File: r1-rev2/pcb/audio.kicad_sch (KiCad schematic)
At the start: 24 parts, among them J4 HP_3.5mm, J5 LO_3.5mm, Q2 AO3401A, Q3 AO3401A, U6 TLV320AIC3104

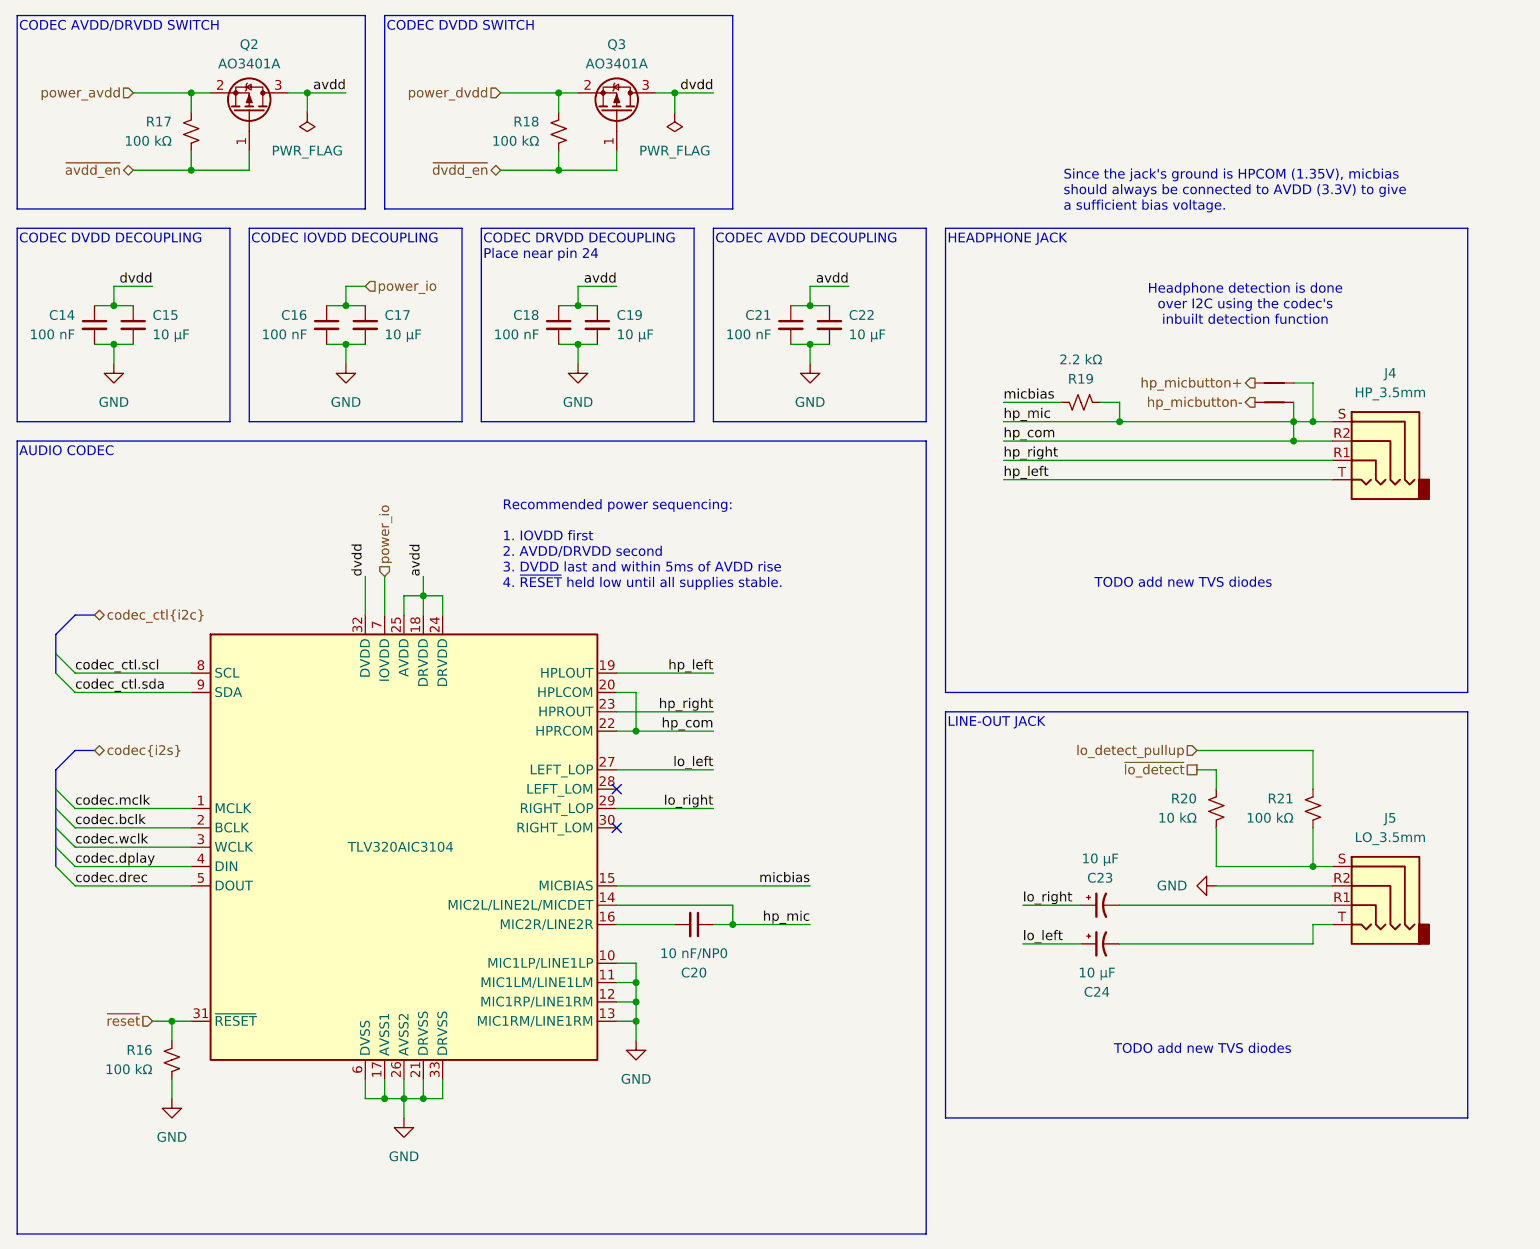
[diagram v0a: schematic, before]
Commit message: R1-Rev2: optimize resistor values
- Resistors used for the ADC dividers were way too high; I didn't
  take into account how the RC constant affected ADC performance
  so the conversion accuracy was probably poor. The new values are
  based on ST's recommendations and the theoretical resolution is
  computed in a spreadsheet.
- Simplify LO detect, originally I had the idea of a "wake on jack
  insert" feature but this is not possible for the headphone jack
  because it is only polled over I2C. The reason for the big 1M
  resistor that was there in Rev1 was to keep the effect on ground
  minimal. If the MCU is powered up then a simple hi-z input with
  internal pullup does the job better.
- Standardize on just 4 unique resistor values to reduce the cost
  of assembly: 5.1k is needed for USB, 2.2k for micbias and battery
  charge reference, and 15k and 68k for voltage reference. Other
  resistors have been rounded to one of these.
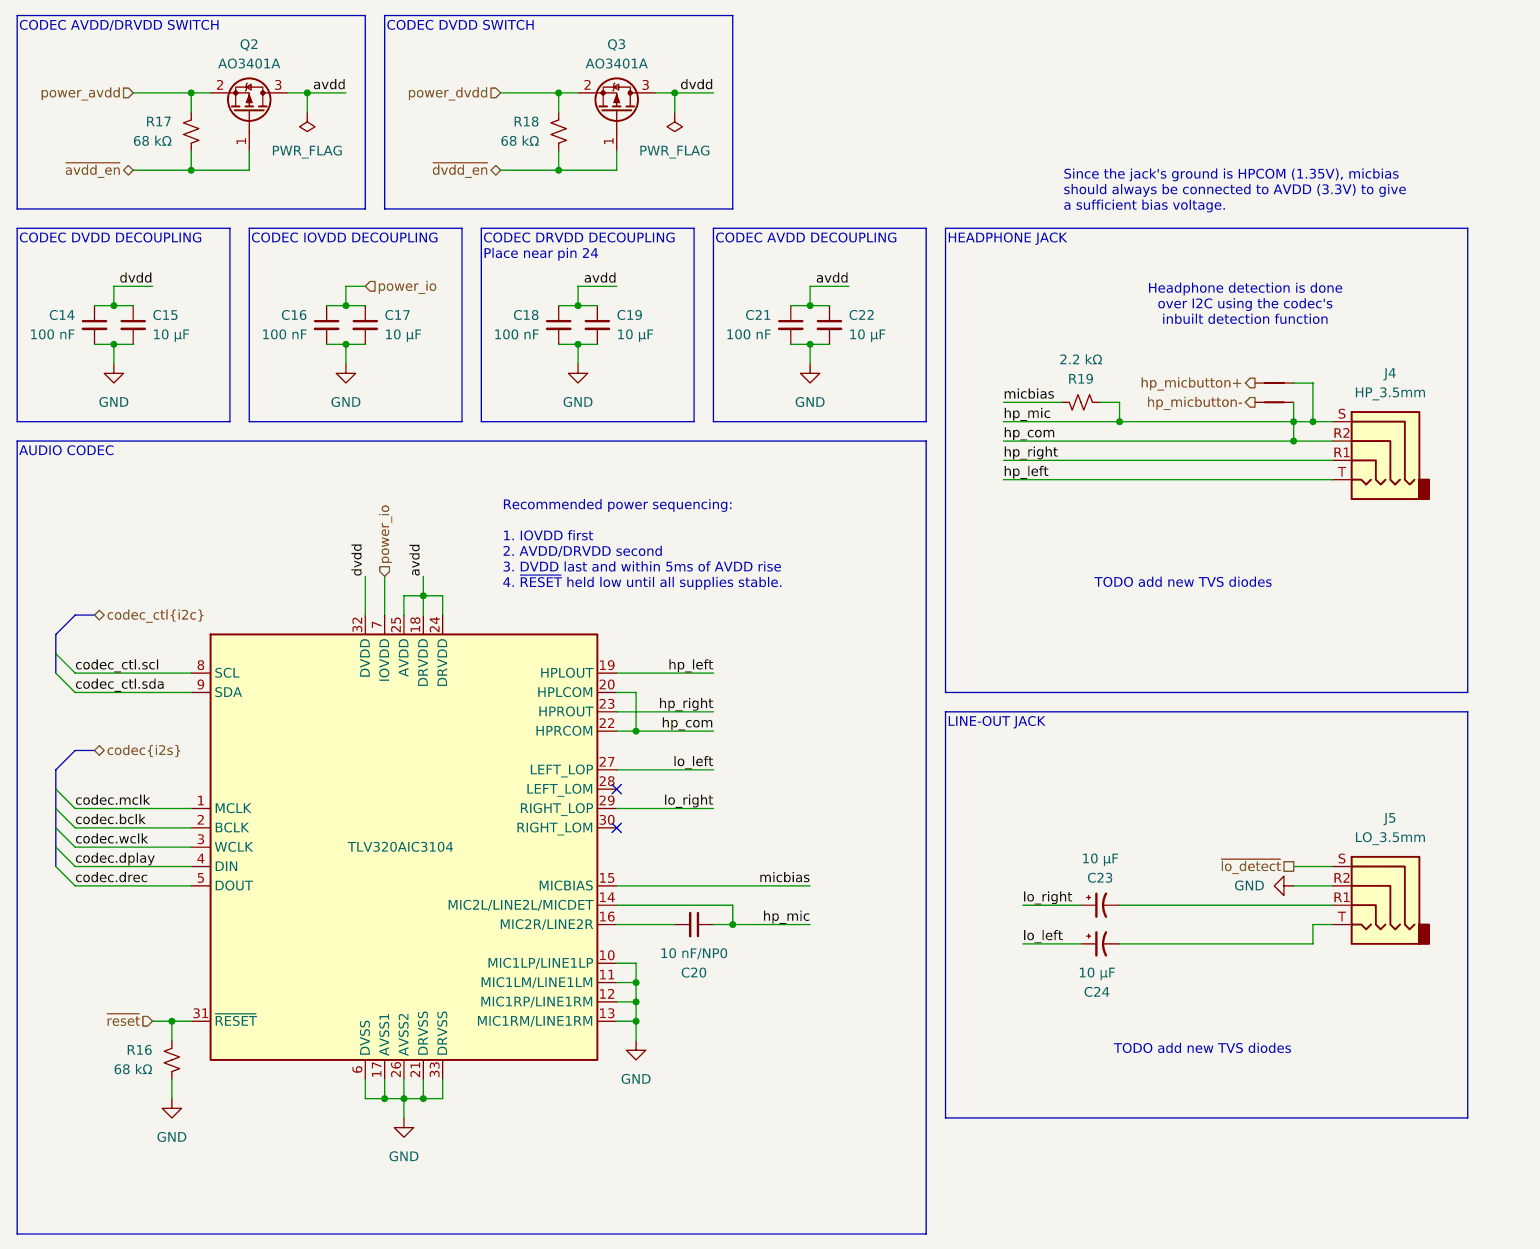
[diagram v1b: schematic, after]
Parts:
- removed R20: 10 kΩ, Resistor_SMD:R_0402_1005Metric, symbol Device:R_Small_US
- removed R21: 100 kΩ, Resistor_SMD:R_0402_1005Metric, symbol Device:R_Small_US
- R16, R17, R18: value 100 kΩ -> 68 kΩ
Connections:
- net ~{lo_detect}: now also J5.S

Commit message: R1-Rev2: strip LCSC part numbers from schematic
These will be managed in a separate BOM spreadsheet going forward.
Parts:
- C14, C16, C18, C21: LCSC# C77020 -> (none)
- C15, C17, C19, C22: LCSC# C91606 -> (none)
- C20: LCSC# C85973 -> (none)
- C23, C24: LCSC# C72485 -> (none)
- J4, J5: LCSC# C5372851 -> (none)
- Q2, Q3: LCSC# C347476 -> (none)
- R16, R17, R18: LCSC# C60491 -> (none)
- R19: LCSC# C114762 -> (none)
- U6: LCSC# C181753 -> (none)
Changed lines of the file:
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@@
-			)
-		)
-		(property "LCSC#" "C77020"
-			(at 93.98 55.88 0)
-			(effects
-				(font
-					(size 1.27 1.27)
-				)
-				(hide yes)
 			)
 		)
@@
 		)
 		(property "Description" "Unpolarized capacitor, small symbol"
-			(at 129.54 55.88 0)
-			(effects
-				(font
-					(size 1.27 1.27)
-				)
-				(hide yes)
-			)
-		)
-		(property "LCSC#" "C91606"
 			(at 129.54 55.88 0)
 			(effects
@@
 			)
 		)
-		(property "LCSC#" "C91606"
-			(at 68.58 55.88 0)
-			(effects
-				(font
-					(size 1.27 1.27)
-				)
-				(hide yes)
-			)
-		)
 		(pin "2"
 		)
@@
 			)
 		)
-		(property "Datasheet" "https://www.lcsc.com/datasheet/lcsc_datasheet_2311091734_UMW-Youtai-Semiconductor-Co---Ltd--AO3401A_C347476.pdf"
+		(property "Datasheet" "~"
 			(at 132.08 27.94 0)
 			(effects
@@
 		)
 		(property "Description" "P-MOSFET transistor, gate/source/drain"
-			(at 132.08 27.94 0)
-			(effects
-				(font
-					(size 1.27 1.27)
-				)
-				(hide yes)
-			)
-		)
-		(property "LCSC#" "C347476"
 			(at 132.08 27.94 0)
 			(effects
@@
 			)
 		)
-		(property "LCSC#" "C91606"
-			(at 99.06 55.88 0)
-			(effects
-				(font
-					(size 1.27 1.27)
-				)
-				(hide yes)
-			)
-		)
 		(pin "2"
 		)
@@
 			)
 		)
-		(property "LCSC#" "C181753"
-			(at 104.14 124.46 0)
-			(effects
-				(font
-					(size 1.27 1.27)
-				)
-				(hide yes)
-			)
-		)
 		(pin "22"
 		)
@@
 			)
 		)
-		(property "LCSC#" "C85973"
-			(at 142.24 134.62 0)
-			(effects
-				(font
-					(size 1.27 1.27)
-				)
-				(hide yes)
-			)
-		)
 		(pin "1"
 		)
@@
 			)
 		)
-		(property "LCSC#" "C72485"
-			(at 195.58 132.08 0)
-			(effects
-				(font
-					(size 1.27 1.27)
-				)
-				(hide yes)
-			)
-		)
 		(pin "1"
 		)
@@
 			)
 		)
-		(property "LCSC#" "C5372851"
-			(at 231.14 71.12 0)
-			(effects
-				(font
-					(size 1.27 1.27)
-				)
-				(hide yes)
-			)
-		)
 		(pin "T"
 		)
@@
 			)
 		)
-		(property "LCSC#" "C77020"
-			(at 154.94 55.88 0)
-			(effects
-				(font
-					(size 1.27 1.27)
-				)
-				(hide yes)
-			)
-		)
 		(pin "2"
 		)
@@
 			)
 		)
-		(property "LCSC#" "C77020"
-			(at 63.5 55.88 0)
-			(effects
-				(font
-					(size 1.27 1.27)
-				)
-				(hide yes)
-			)
-		)
 		(pin "2"
 		)
@@
 			)
 		)
-		(property "LCSC#" "C60491"
-			(at 124.46 30.48 0)
-			(effects
-				(font
-					(size 1.27 1.27)
-				)
-				(hide yes)
-			)
-		)
 		(pin "1"
 		)
@@
 			)
 		)
-		(property "LCSC#" "C72485"
-			(at 195.58 137.16 0)
-			(effects
-				(font
-					(size 1.27 1.27)
-				)
-				(hide yes)
-			)
-		)
 		(pin "1"
 		)
@@
 			)
 		)
-		(property "LCSC#" "C60491"
-			(at 76.2 30.48 0)
-			(effects
-				(font
-					(size 1.27 1.27)
-				)
-				(hide yes)
-			)
-		)
 		(pin "1"
 		)
@@
 			)
 		)
-		(property "LCSC#" "C5372851"
-			(at 231.14 129.54 0)
-			(effects
-				(font
-					(size 1.27 1.27)
-				)
-				(hide yes)
-			)
-		)
 		(pin "T"
 		)
@@
 		)
 		(property "Description" "Unpolarized capacitor, small symbol"
-			(at 160.02 55.88 0)
-			(effects
-				(font
-					(size 1.27 1.27)
-				)
-				(hide yes)
-			)
-		)
-		(property "LCSC#" "C91606"
 			(at 160.02 55.88 0)
 			(effects
@@
 			)
 		)
-		(property "LCSC#" "C114762"
-			(at 193.04 66.04 0)
-			(effects
-				(font
-					(size 1.27 1.27)
-				)
-				(hide yes)
-			)
-		)
 		(pin "2"
 		)
@@
 			)
 		)
-		(property "LCSC#" "C77020"
-			(at 124.46 55.88 0)
-			(effects
-				(font
-					(size 1.27 1.27)
-				)
-				(hide yes)
-			)
-		)
 		(pin "2"
 		)
@@
 			)
 		)
-		(property "Datasheet" "https://www.lcsc.com/datasheet/lcsc_datasheet_2311091734_UMW-Youtai-Semiconductor-Co---Ltd--AO3401A_C347476.pdf"
+		(property "Datasheet" "~"
 			(at 83.82 27.94 0)
 			(effects
@@
 		)
 		(property "Description" "P-MOSFET transistor, gate/source/drain"
-			(at 83.82 27.94 0)
-			(effects
-				(font
-					(size 1.27 1.27)
-				)
-				(hide yes)
-			)
-		)
-		(property "LCSC#" "C347476"
 			(at 83.82 27.94 0)
 			(effects
@@
 			(at 73.66 152.4 0)
 			(effects
-				(font
-					(size 1.27 1.27)
-				)
-				(hide yes)
-			)
-		)
-		(property "LCSC#" "C60491"
-			(at 73.66 152.4 0)
-			(effects

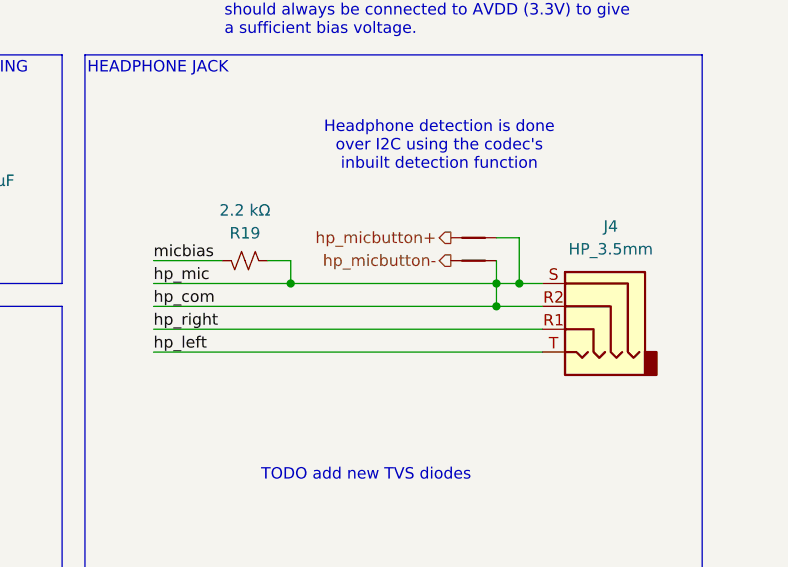
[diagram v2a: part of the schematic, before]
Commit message: R1-Rev2: finish STM32 pin assignment and fix ERC issues
- Expanded LCD bus from 8 to 16 pins so it can be accessed by DMA2D.
- Added RDX pin to LCD bus to allow read access
- Added UART console port for easier access to debug logging
- Shorted USB HS and FS PHYs for DFU mode support
- Connected all GPIOs and peripheral pins
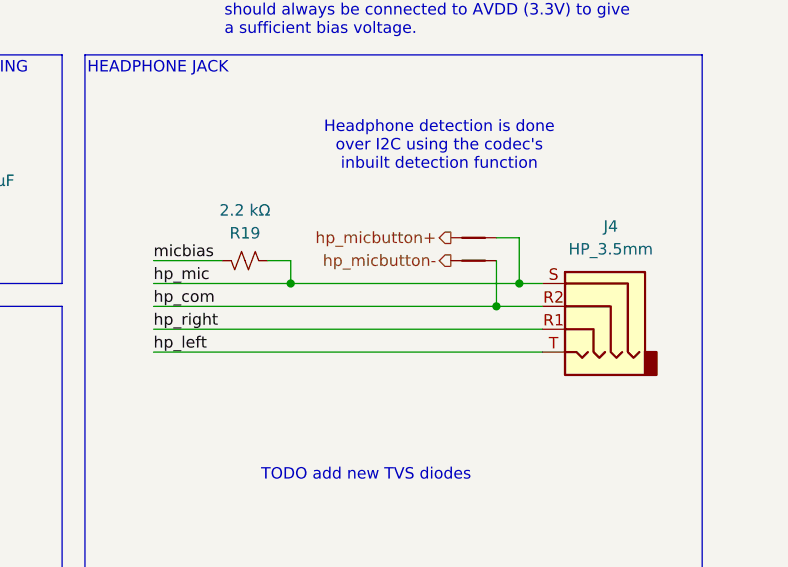
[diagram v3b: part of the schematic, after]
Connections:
- net hp_com: no longer C20.1, J4.S, NT1.2, R19.2, U6.14 (MIC2L/LINE2L/MICDET)
- new net hp_mic: C20.1, J4.S, NT1.2, R19.2, U6.14 (MIC2L/LINE2L/MICDET)
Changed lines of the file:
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@@
+	)
+	(junction
+		(at 147.32 134.62)
+		(diameter 0)
+		(color 0 0 0 0)
+	)
+	(junction
+		(at 76.2 35.56)
+		(diameter 0)
+		(color 0 0 0 0)
+	)
+	(junction
+		(at 96.52 53.34)
+		(diameter 0)
+		(color 0 0 0 0)
+	)
+	(junction
+		(at 104.14 157.48)
+		(diameter 0)
+		(color 0 0 0 0)
+	)
+	(junction
+		(at 66.04 58.42)
+		(diameter 0)
+		(color 0 0 0 0)
+	)
+	(junction
+		(at 106.68 91.44)
+		(diameter 0)
+		(color 0 0 0 0)
+	)
+	(junction
+		(at 73.66 147.32)
+		(diameter 0)
+		(color 0 0 0 0)
+	)
+	(junction
+		(at 134.62 147.32)
+		(diameter 0)
+		(color 0 0 0 0)
+	)
+	(junction
+		(at 96.52 58.42)
+		(diameter 0)
+		(color 0 0 0 0)
+	)
+	(junction
+		(at 223.52 68.58)
+		(diameter 0)
+		(color 0 0 0 0)
+	)
+	(junction
+		(at 66.04 53.34)
+		(diameter 0)
+		(color 0 0 0 0)
+	)
+	(junction
+		(at 124.46 25.4)
+		(diameter 0)
+		(color 0 0 0 0)
+	)
+	(junction
+		(at 127 53.34)
+		(diameter 0)
+		(color 0 0 0 0)
+	)
+	(junction
+		(at 76.2 25.4)
+		(diameter 0)
+		(color 0 0 0 0)
+	)
+	(junction
+		(at 127 58.42)
+		(diameter 0)
+		(color 0 0 0 0)
+	)
+	(junction
+		(at 134.62 142.24)
+		(diameter 0)
+		(color 0 0 0 0)
+	)
+	(junction
+		(at 106.68 157.48)
+		(diameter 0)
+		(color 0 0 0 0)
+	)
+	(junction
+		(at 157.48 53.34)
+		(diameter 0)
+		(color 0 0 0 0)
 	)
 	(junction
@@
 	)
 	(junction
-		(at 147.32 134.62)
-		(diameter 0)
-		(color 0 0 0 0)
-	)
-	(junction
-		(at 76.2 35.56)
-		(diameter 0)
-		(color 0 0 0 0)
-	)
-	(junction
-		(at 96.52 53.34)
-		(diameter 0)
-		(color 0 0 0 0)
-	)
-	(junction
-		(at 104.14 157.48)
-		(diameter 0)
-		(color 0 0 0 0)
-	)
-	(junction
-		(at 66.04 58.42)
-		(diameter 0)
-		(color 0 0 0 0)
-	)
-	(junction
-		(at 106.68 91.44)
-		(diameter 0)
-		(color 0 0 0 0)
-	)
-	(junction
-		(at 73.66 147.32)
-		(diameter 0)
-		(color 0 0 0 0)
-	)
-	(junction
-		(at 134.62 147.32)
-		(diameter 0)
-		(color 0 0 0 0)
-	)
-	(junction
-		(at 96.52 58.42)
-		(diameter 0)
-		(color 0 0 0 0)
-	)
-	(junction
-		(at 223.52 68.58)
-		(diameter 0)
-		(color 0 0 0 0)
-	)
-	(junction
-		(at 66.04 53.34)
-		(diameter 0)
-		(color 0 0 0 0)
-	)
-	(junction
-		(at 124.46 25.4)
-		(diameter 0)
-		(color 0 0 0 0)
-	)
-	(junction
-		(at 127 53.34)
-		(diameter 0)
-		(color 0 0 0 0)
-	)
-	(junction
-		(at 76.2 25.4)
-		(diameter 0)
-		(color 0 0 0 0)
-	)
-	(junction
-		(at 127 58.42)
-		(diameter 0)
-		(color 0 0 0 0)
-	)
-	(junction
-		(at 134.62 142.24)
-		(diameter 0)
-		(color 0 0 0 0)
-	)
-	(junction
-		(at 106.68 157.48)
-		(diameter 0)
-		(color 0 0 0 0)
-	)
-	(junction
-		(at 157.48 53.34)
-		(diameter 0)
-		(color 0 0 0 0)
-	)
-	(junction
 		(at 101.6 157.48)
 		(diameter 0)
@@
 	(junction
 		(at 134.62 144.78)
-		(diameter 0)
-		(color 0 0 0 0)
-	)
-	(junction
-		(at 220.98 68.58)
 		(diameter 0)
 		(color 0 0 0 0)
@@
 	(wire
 		(pts
+			(xy 220.98 71.12) (xy 226.06 71.12)
+		)
+		(stroke
+			(width 0)
+			(type default)
+		)
+	)
+	(wire
+		(pts
 			(xy 220.98 129.54) (xy 226.06 129.54)
 		)
@@
 		)
 	)
-	(wire
-		(pts
-			(xy 220.98 66.04) (xy 220.98 68.58)
-		)
-		(stroke
-			(width 0)
-			(type default)
-		)
-	)
 	(bus
 		(pts
@@
 	(wire
 		(pts
+			(xy 220.98 66.04) (xy 220.98 71.12)
+		)
+		(stroke
+			(width 0)
+			(type default)
+		)
+	)
+	(wire
+		(pts
 			(xy 109.22 157.48) (xy 106.68 157.48)
 		)
@@
 	(wire
 		(pts
-			(xy 198.12 68.58) (xy 220.98 68.58)
-		)
-		(stroke
-			(width 0)
-			(type default)
-		)
-	)
-	(wire
-		(pts
-			(xy 220.98 71.12) (xy 226.06 71.12)
+			(xy 198.12 68.58) (xy 223.52 68.58)
+		)
+		(stroke
+			(width 0)
+			(type default)
+		)
+	)
+	(wire
+		(pts
+			(xy 182.88 71.12) (xy 220.98 71.12)
 		)
 		(stroke
@@
 	(wire
 		(pts
-			(xy 182.88 71.12) (xy 220.98 71.12)
-		)
-		(stroke
-			(width 0)
-			(type default)
-		)
-	)
-	(wire
-		(pts
 			(xy 132.08 139.7) (xy 134.62 139.7)
 		)
@@
 	(wire
 		(pts
-			(xy 223.52 68.58) (xy 220.98 68.58)
-		)
-		(stroke
-			(width 0)
-			(type default)
-		)
-	)
-	(wire
-		(pts
 			(xy 60.96 119.38) (xy 76.2 119.38)
 		)
@@
 		)
 		(stroke
-			(width 0)
-			(type default)
-		)
-	)
-	(wire
-		(pts
-			(xy 220.98 68.58) (xy 220.98 71.12)
-		)
-		(stroke
